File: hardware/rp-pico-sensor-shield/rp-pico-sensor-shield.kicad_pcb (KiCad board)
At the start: 2 copper layers, 87 x 65 mm, 36 parts, among them J1 Barrel_Jack, J10 Conn_01x04, J11 Conn_01x04, J12 Conn_01x04, J13 Conn_01x04, J14 Conn_01x04, J15 Conn_01x04, J16 Conn_01x04, J17 Conn_01x04, J18 Conn_01x03, J19 Conn_01x03, J2 AGND, J20 Conn_01x03, J21 Conn_01x03, J22 Conn_01x03, J23 Conn_01x03, J24 SM04B-SRSS-TB, J25 Conn_01x04, J26 Conn_01x04, J27 Conn_01x03, J3 Conn_01x04, J4 Conn_01x04, J5 Conn_01x04, J6 Conn_01x04, J7 Conn_01x04, J8 Conn_01x04, J9 Conn_01x04, Q1 DMG2305UX, SW1 SW_Push, U1 Pico, U2 NCP1117-5.0_SOT223

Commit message: tweaks
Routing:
- net GND: track 448.1 -> 461.9 mm, vias 0 -> 1
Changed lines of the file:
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@@
   )
   (segment (start 117.6113 77.1685) (end 113.7798 81) (width 0.8) (layer "F.Cu") (net 1))
-  (segment (start 117.6113 76.631) (end 117.6113 77.1685) (width 0.8) (layer "F.Cu") (net 1))
+  (segment (start 117.6113 77.1685) (end 117.6113 76.631) (width 0.8) (layer "F.Cu") (net 1))
+  (segment (start 117.6113 76.631) (end 123.3586 70.8837) (width 0.8) (layer "F.Cu") (net 1))
   (segment (start 113.7798 81) (end 113.3048 81) (width 0.8) (layer "F.Cu") (net 1))
-  (segment (start 117.6113 76.631) (end 123.3586 70.8837) (width 0.8) (layer "F.Cu") (net 1))
   (segment (start 113.4214 76.631) (end 117.6113 76.631) (width 0.8) (layer "F.Cu") (net 1))
   (segment (start 107.696 80.6516) (end 108.8852 79.4624) (width 0.5) (layer "F.Cu") (net 2))
-  (segment (start 122.936 82.55) (end 122.301 83.185) (width 0.5) (layer "F.Cu") (net 2))
   (segment (start 109.728 82.55) (end 108.204 82.55) (width 0.5) (layer "F.Cu") (net 2))
-  (segment (start 122.301 83.185) (end 122.301 87.757) (width 0.5) (layer "F.Cu") (net 2))
   (segment (start 132.969 97.902) (end 132.371 98.5) (width 0.5) (layer "F.Cu") (net 2))
-  (segment (start 132.969 92.583) (end 132.969 97.902) (width 0.5) (layer "F.Cu") (net 2))
+  (segment (start 132.969 92.583) (end 132.969 97.79) (width 0.5) (layer "F.Cu") (net 2))
   (segment (start 132.371 98.5) (end 131.0963 98.5) (width 0.5) (layer "F.Cu") (net 2))
-  (segment (start 113.3048 79.45) (end 112.828 79.45) (width 0.5) (layer "F.Cu") (net 2))
+  (segment (start 108.8852 78.3128) (end 108.8852 76.6948) (width 0.5) (layer "F.Cu") (net 2))
   (segment (start 131.318 90.932) (end 132.969 92.583) (width 0.5) (layer "F.Cu") (net 2))
   (segment (start 68.8808 73.66) (end 69.6184 74.3976) (width 0.8) (layer "F.Cu") (net 2))
   (segment (start 57.656 73.66) (end 68.8808 73.66) (width 0.8) (layer "F.Cu") (net 2))
-  (segment (start 122.936 82.55) (end 123.486 82) (width 0.5) (layer "F.Cu") (net 2))
+  (segment (start 125.6548 82) (end 122.301 85.3538) (width 0.8) (layer "F.Cu") (net 2))
   (segment (start 69.6184 74.3976) (end 69.6184 76.0476) (width 0.8) (layer "F.Cu") (net 2))
   (segment (start 125.476 90.932) (end 131.318 90.932) (width 0.5) (layer "F.Cu") (net 2))
+  (segment (start 122.301 85.3538) (end 122.301 86.741) (width 0.8) (layer "F.Cu") (net 2))
+  (segment (start 129.3586 70.8837) (end 129.3586 78.2962) (width 0.8) (layer "F.Cu") (net 2))
+  (segment (start 129.3586 78.2962) (end 125.6548 82) (width 0.8) (layer "F.Cu") (net 2))
   (segment (start 108.204 82.55) (end 107.696 82.042) (width 0.5) (layer "F.Cu") (net 2))
   (segment (start 56.9184 74.3976) (end 57.656 73.66) (width 0.8) (layer "F.Cu") (net 2))
-  (segment (start 123.486 82) (end 125.6548 82) (width 0.5) (layer "F.Cu") (net 2))
+  (segment (start 109.877999 82.400001) (end 112.828 79.45) (width 0.8) (layer "F.Cu") (net 2))
   (segment (start 122.301 87.757) (end 125.476 90.932) (width 0.5) (layer "F.Cu") (net 2))
-  (segment (start 108.8852 79.4624) (end 108.8852 76.6948) (width 0.5) (layer "F.Cu") (net 2))
-  (segment (start 112.828 79.45) (end 109.728 82.55) (width 0.5) (layer "F.Cu") (net 2))
+  (segment (start 122.301 86.741) (end 122.301 87.757) (width 0.5) (layer "F.Cu") (net 2))
+  (segment (start 108.8852 79.4624) (end 108.8852 78.4052) (width 0.5) (layer "F.Cu") (net 2))
+  (segment (start 107.696 81.534) (end 107.696 80.6516) (width 0.5) (layer "F.Cu") (net 2))
+  (segment (start 125.254799 82.400001) (end 109.877999 82.400001) (width 0.8) (layer "F.Cu") (net 2))
   (segment (start 108.8852 76.6948) (end 108.8214 76.631) (width 0.5) (layer "F.Cu") (net 2))
-  (segment (start 107.696 82.042) (end 107.696 80.6516) (width 0.5) (layer "F.Cu") (net 2))
-  (segment (start 109.728 82.55) (end 122.936 82.55) (width 0.5) (layer "F.Cu") (net 2))
+  (segment (start 132.969 97.79) (end 132.969 97.902) (width 0.5) (layer "F.Cu") (net 2))
+  (segment (start 107.696 82.042) (end 107.696 81.534) (width 0.5) (layer "F.Cu") (net 2))
+  (segment (start 112.828 79.45) (end 113.3048 79.45) (width 0.8) (layer "F.Cu") (net 2))
   (segment (start 56.9184 76.0476) (end 56.9184 74.3976) (width 0.8) (layer "F.Cu") (net 2))
+  (segment (start 125.6548 82) (end 125.254799 82.400001) (width 0.8) (layer "F.Cu") (net 2))
+  (via (at 122.301 86.741) (size 0.8) (drill 0.4) (layers "F.Cu" "B.Cu") (net 2))
   (segment (start 124.206 113.411) (end 133.35 104.267) (width 0.8) (layer "B.Cu") (net 2))
   (segment (start 129.3586 70.8837) (end 129.3586 78.0838) (width 0.8) (layer "B.Cu") (net 2))
@@
   (segment (start 107.851919 83.400001) (end 112.229 83.4) (width 0.8) (layer "F.Cu") (net 9))
   (segment (start 106.426 65.184032) (end 106.426 81.974082) (width 0.8) (layer "F.Cu") (net 9))
+  (segment (start 110.2654 105.54) (end 107.7254 105.54) (width 0.8) (layer "F.Cu") (net 9))
   (segment (start 64.008 54.102) (end 65.19 52.92) (width 0.8) (layer "F.Cu") (net 9))
   (segment (start 89.905 90.54) (end 81.7254 90.54) (width 0.8) (layer "B.Cu") (net 9))
@@
   (segment (start 81.7254 105.54) (end 79.1854 105.54) (width 0.8) (layer "B.Cu") (net 9))
   (segment (start 76.6454 105.54) (end 71.2654 105.54) (width 0.8) (layer "B.Cu") (net 9))
-  (segment (start 110.2654 105.54) (end 107.7254 105.54) (width 0.8) (layer "B.Cu") (net 9))
   (segment (start 79.1854 90.54) (end 81.7254 90.54) (width 0.8) (layer "B.Cu") (net 9))
   (segment (start 111.125 96.012) (end 95.377 96.012) (width 0.8) (layer "B.Cu") (net 9))
@@
   (segment (start 94.049 84.143) (end 92.4784 82.5724) (width 0.25) (layer "F.Cu") (net 19))
   (segment (start 94.499 84.963) (end 97.5584 81.9036) (width 0.25) (layer "F.Cu") (net 20))
+  (segment (start 104.873 106.905) (end 103.886 105.918) (width 0.25) (layer "F.Cu") (net 20))
+  (segment (start 101.473 99.820604) (end 99.569396 99.820604) (width 0.25) (layer "F.Cu") (net 20))
+  (segment (start 106.5504 106.905) (end 104.873 106.905) (width 0.25) (layer "F.Cu") (net 20))
   (segment (start 97.5584 81.9036) (end 97.5584 76.0476) (width 0.25) (layer "F.Cu") (net 20))
   (segment (start 94.499 94.750208) (end 94.499 84.963) (width 0.25) (layer "F.Cu") (net 20))
   (segment (start 99.569396 99.820604) (end 94.499 94.750208) (width 0.25) (layer "F.Cu") (net 20))
-  (segment (start 107.7254 108.08) (end 106.3604 106.715) (width 0.25) (layer "F.Cu") (net 20))
-  (segment (start 106.3604 106.715) (end 106.3604 102.513299) (width 0.25) (layer "F.Cu") (net 20))
-  (segment (start 103.667705 99.820604) (end 99.569396 99.820604) (width 0.25) (layer "F.Cu") (net 20))
-  (segment (start 106.3604 102.513299) (end 103.667705 99.820604) (width 0.25) (layer "F.Cu") (net 20))
+  (segment (start 107.7254 108.08) (end 106.5504 106.905) (width 0.25) (layer "F.Cu") (net 20))
+  (segment (start 103.886 105.918) (end 103.886 101.979604) (width 0.25) (layer "F.Cu") (net 20))
+  (segment (start 103.886 101.979604) (end 101.727 99.820604) (width 0.25) (layer "F.Cu") (net 20))
+  (segment (start 101.727 99.820604) (end 101.473 99.820604) (width 0.25) (layer "F.Cu") (net 20))
   (segment (start 94.949 94.563812) (end 94.949 85.149396) (width 0.25) (layer "F.Cu") (net 21))
-  (segment (start 109.0904 102.703299) (end 105.757705 99.370604) (width 0.25) (layer "F.Cu") (net 21))
-  (segment (start 105.757705 99.370604) (end 99.755792 99.370604) (width 0.25) (layer "F.Cu") (net 21))
-  (segment (start 109.0904 106.905) (end 109.0904 102.703299) (width 0.25) (layer "F.Cu") (net 21))
+  (segment (start 107.186796 106.905) (end 106.426 106.144204) (width 0.25) (layer "F.Cu") (net 21))
+  (segment (start 109.0904 106.905) (end 107.186796 106.905) (width 0.25) (layer "F.Cu") (net 21))
+  (segment (start 103.217705 99.370604) (end 99.755792 99.370604) (width 0.25) (layer "F.Cu") (net 21))
+  (segment (start 106.426 102.578899) (end 103.217705 99.370604) (width 0.25) (layer "F.Cu") (net 21))
+  (segment (start 106.426 106.144204) (end 106.426 102.578899) (width 0.25) (layer "F.Cu") (net 21))
+  (segment (start 94.949 85.149396) (end 100.0984 79.999996) (width 0.25) (layer "F.Cu") (net 21))
   (segment (start 110.2654 108.08) (end 109.0904 106.905) (width 0.25) (layer "F.Cu") (net 21))
-  (segment (start 94.949 85.149396) (end 100.0984 79.999996) (width 0.25) (layer "F.Cu") (net 21))
   (segment (start 100.0984 79.999996) (end 100.0984 76.0476) (width 0.25) (layer "F.Cu") (net 21))
   (segment (start 99.755792 99.370604) (end 94.949 94.563812) (width 0.25) (layer "F.Cu") (net 21))

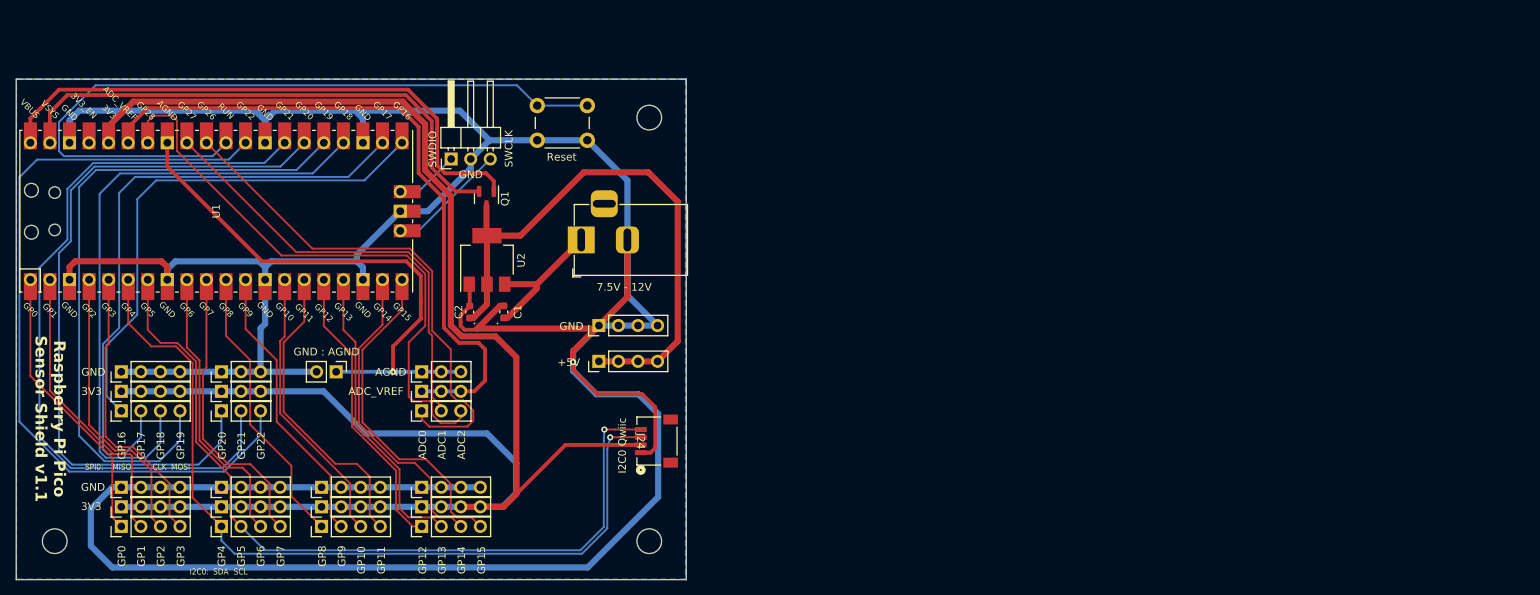
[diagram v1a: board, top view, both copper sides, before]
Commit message: finalized pin wiring
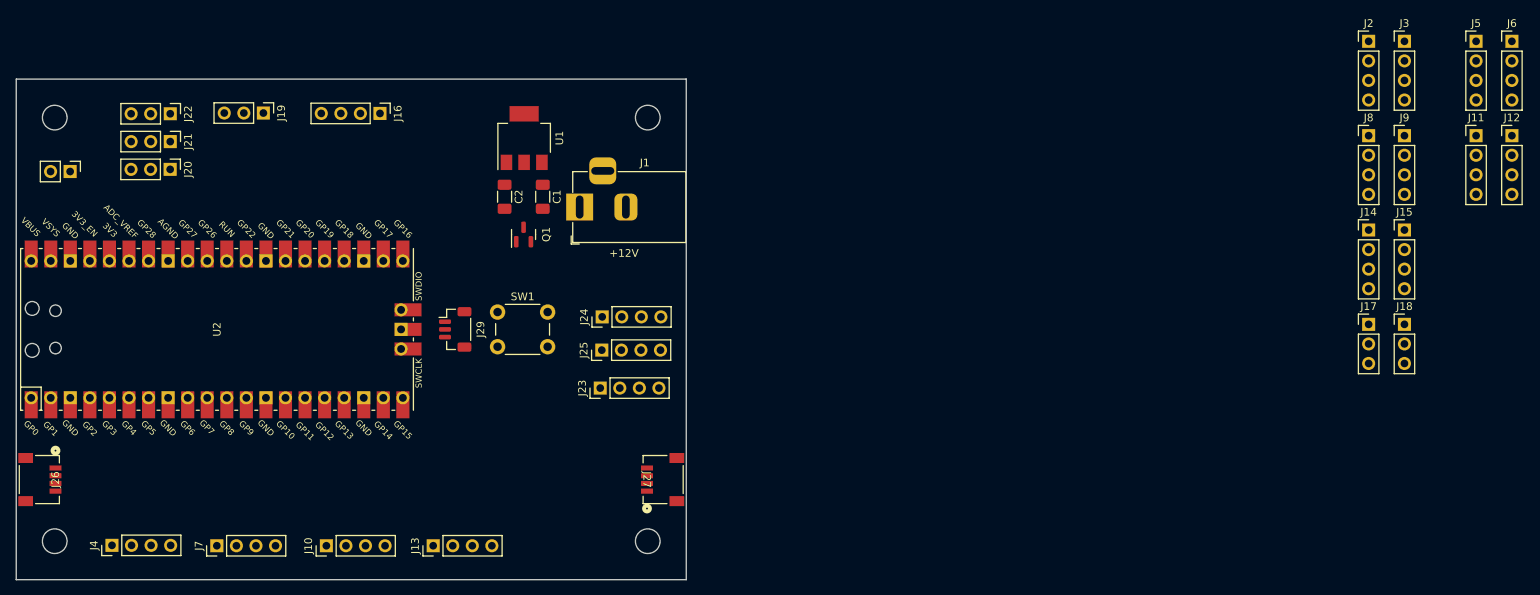
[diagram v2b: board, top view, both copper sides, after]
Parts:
- removed the REF** at (132.2, 110.0)
- removed the REF** at (132.2, 55.0)
- added J28: AGND, Connector_PinHeader_2.54mm:PinHeader_1x02_P2.54mm_Vertical, F.Cu at (57.0, 62.0)
- added J29: Conn_01x03, Connector_JST:JST_SH_BM03B-SRSS-TB_1x03-1MP_P1.00mm_Vertical, F.Cu at (107.0, 82.5)
- added REF**: MountingHole_3.2mm_M3, MountingHole:MountingHole_3.2mm_M3, F.Cu at (55.0, 55.0)
- added REF**: MountingHole_3.2mm_M3, MountingHole:MountingHole_3.2mm_M3, F.Cu at (132.0, 110.0)
- added REF**: MountingHole_3.2mm_M3, MountingHole:MountingHole_3.2mm_M3, F.Cu at (132.0, 55.0)
- C1, C2: footprint Capacitor_SMD:C_0603_1608Metric -> Capacitor_SMD:C_1206_3216Metric_Pad1.33x1.80mm_HandSolder
- J17: value Conn_01x04 -> Conn_01x03; footprint Connector_PinHeader_2.54mm:PinHeader_1x04_P2.54mm_Vertical -> Connector_PinHeader_2.54mm:PinHeader_1x03_P2.54mm_Vertical
- J2: value AGND -> Conn_01x04; footprint Connector_PinHeader_2.54mm:PinHeader_1x02_P2.54mm_Vertical -> Connector_PinHeader_2.54mm:PinHeader_1x04_P2.54mm_Vertical
- J23: value Conn_01x03 -> Conn_01x04; footprint Connector_PinHeader_2.54mm:PinHeader_1x03_P2.54mm_Vertical -> Connector_PinHeader_2.54mm:PinHeader_1x04_P2.54mm_Vertical
- J24: value SM04B-SRSS-TB -> Conn_01x04; footprint SM04B-SRSS-TB:CONN_SM04B-SRSS-TB_JST -> Connector_PinHeader_2.54mm:PinHeader_1x04_P2.54mm_Vertical
- J26: value Conn_01x04 -> I2C0; footprint Connector_PinHeader_2.54mm:PinHeader_1x04_P2.54mm_Vertical -> SM04B-SRSS-TB:CONN_SM04B-SRSS-TB_JST
- J27: value Conn_01x03 -> I2C1; footprint Connector_PinHeader_2.54mm:PinHeader_1x03_P2.54mm_Horizontal -> SM04B-SRSS-TB:CONN_SM04B-SRSS-TB_JST
- U1: value Pico -> NCP1117-5.0_SOT223; footprint MCU_RaspberryPi_and_Boards:RPi_Pico_SMD_TH -> Package_TO_SOT_SMD:SOT-223-3_TabPin2
- U2: value NCP1117-5.0_SOT223 -> Pico; footprint Package_TO_SOT_SMD:SOT-223-3_TabPin2 -> MCU_RaspberryPi_and_Boards:RPi_Pico_SMD_TH
- moved J5 185.2 mm to (239.6, 45.1), turned to 0 degrees
- moved J3 178.1 mm to (230.3, 45.1), turned to 0 degrees
- moved J6 177.3 mm to (244.2, 45.1), turned to 0 degrees
- moved J15 167.6 mm to (230.3, 69.6), turned to 0 degrees
- moved J17 162.3 mm to (225.6, 81.8), turned to 0 degrees
- moved J11 158.3 mm to (239.6, 57.3), turned to 0 degrees
- moved J8 157.4 mm to (225.6, 57.3), turned to 0 degrees
- moved J18 154.0 mm to (230.3, 81.8), turned to 0 degrees
- moved J12 148.7 mm to (244.2, 57.3), turned to 0 degrees
- moved J9 147.8 mm to (230.3, 57.3), turned to 0 degrees
- moved J2 140.8 mm to (225.6, 45.1), turned to 0 degrees
- moved J14 128.8 mm to (225.6, 69.6), turned to 0 degrees
- moved J26 75.4 mm to (53.0, 102.0)
- moved J27 49.9 mm to (134.0, 102.0), turned to -90 degrees
- moved J16 49.3 mm to (97.2, 54.5), turned to -90 degrees
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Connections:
- C1 pad 1: Net-(U2-VI) -> +12V
- J1 pad 1: Net-(U2-VI) -> +12V
- J10 pad 1: +3.3V -> GPIO8
- J10 pad 2: +3.3V -> GPIO9
- J10 pad 3: +3.3V -> GPIO10
- J10 pad 4: +3.3V -> GPIO11
- J11 pad 1: GPIO8 -> GND
- J11 pad 2: GPIO9 -> GND
- J11 pad 3: GPIO10 -> GND
- J11 pad 4: GPIO11 -> GND
- J12 pad 1: GND -> +3.3V
- J12 pad 2: GND -> +3.3V
- J12 pad 3: GND -> +3.3V
- J12 pad 4: GND -> +3.3V
- J13 pad 1: +3.3V -> GPIO12
- J13 pad 2: +3.3V -> GPIO13
- J13 pad 3: +3.3V -> GPIO14
- J13 pad 4: +3.3V -> GPIO15
- J14 pad 1: GPIO12 -> GND
- J14 pad 2: GPIO13 -> GND
- J14 pad 3: GPIO14 -> GND
- J14 pad 4: GPIO15 -> GND
- J15 pad 1: GND -> +3.3V
- J15 pad 2: GND -> +3.3V
- J15 pad 3: GND -> +3.3V
- J15 pad 4: GND -> +3.3V
- J16 pad 1: +3.3V -> GPIO16
- J16 pad 2: +3.3V -> GPIO17
- J16 pad 3: +3.3V -> GPIO18
- J16 pad 4: +3.3V -> GPIO19
- J17 pad 1: GPIO16 -> GND
- J17 pad 2: GPIO17 -> GND
- J17 pad 3: GPIO18 -> GND
- J18 pad 1: GPIO20 -> +3.3V
- J18 pad 2: GPIO21 -> +3.3V
- J18 pad 3: GPIO22 -> +3.3V
- J19 pad 1: +3.3V -> GPIO20
- J19 pad 2: +3.3V -> GPIO21
- J19 pad 3: +3.3V -> GPIO22
- J2 pad 1: AGND -> GND
- J20 pad 1: GND -> AGND
- J20 pad 2: GND -> AGND
- J20 pad 3: GND -> AGND
- J21 pad 1: AGND -> ADC_VREF
- J21 pad 2: AGND -> ADC_VREF
- J21 pad 3: AGND -> ADC_VREF
- J22 pad 1: ADC_VREF -> ADC0
- J22 pad 2: ADC_VREF -> ADC1
- J22 pad 3: ADC_VREF -> ADC2
- J23 pad 1: ADC0 -> GND
- J23 pad 2: ADC1 -> GND
- J23 pad 3: ADC2 -> GND
- J24 pad 1: GND -> +12V
- J24 pad 2: +3.3V -> +12V
- J24 pad 3: GPIO4 -> +12V
- J24 pad 4: GPIO5 -> +12V
- J26 pad 2: GND -> +3.3V
- J26 pad 3: GND -> GPIO4
- J26 pad 4: GND -> GPIO5
- J27 pad 1: SWIO -> GND
- J27 pad 2: GND -> +3.3V
- J27 pad 3: SWCLK -> GPIO6
- J3 pad 1: GPIO0 -> +3.3V
- J3 pad 2: GPIO1 -> +3.3V
- J3 pad 3: GPIO2 -> +3.3V
- J3 pad 4: GPIO3 -> +3.3V
- J4 pad 1: +3.3V -> GPIO0
- J4 pad 2: +3.3V -> GPIO1
- J4 pad 3: +3.3V -> GPIO2
- J4 pad 4: +3.3V -> GPIO3
- J6 pad 1: GND -> +3.3V
- J6 pad 2: GND -> +3.3V
- J6 pad 3: GND -> +3.3V
- J6 pad 4: GND -> +3.3V
- J7 pad 1: +3.3V -> GPIO4
- J7 pad 2: +3.3V -> GPIO5
- J7 pad 3: +3.3V -> GPIO6
- J7 pad 4: +3.3V -> GPIO7
- J8 pad 1: GPIO4 -> GND
- J8 pad 2: GPIO5 -> GND
- J8 pad 3: GPIO6 -> GND
- J8 pad 4: GPIO7 -> GND
- J9 pad 1: GND -> +3.3V
- J9 pad 2: GND -> +3.3V
- J9 pad 3: GND -> +3.3V
- J9 pad 4: GND -> +3.3V
- U1 pad 1: GPIO0 -> GND
- U1 pad 2: GPIO1 -> +5V
- U1 pad 3: GND -> +12V
- U2 pad 1: GND -> GPIO0
- U2 pad 2: +5V -> GPIO1
- U2 pad 3: Net-(U2-VI) -> GND
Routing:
- net GND: track 461.9 -> 0.00 mm, vias 1 -> 0
- net +3.3V: track 236.6 -> 0.00 mm
- net GPIO4: track 108.8 -> 0.00 mm, vias 1 -> 0
- net GPIO5: track 105.3 -> 0.00 mm, vias 1 -> 0
- net GPIO22: track 102.0 -> 0.00 mm
- net GPIO21: track 98.3 -> 0.00 mm
- net RESET: track 98.1 -> 0.00 mm
- net GPIO20: track 94.4 -> 0.00 mm
- net ADC_VREF: track 88.5 -> 0.00 mm
- net GPIO19: track 85.9 -> 0.00 mm
- net GPIO18: track 81.0 -> 0.00 mm
- net GPIO17: track 80.6 -> 0.00 mm
- net ADC2: track 77.0 -> 0.00 mm
- net +5V: track 75.0 -> 0.00 mm
- net Net-(Q1-G): track 74.7 -> 0.00 mm
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- removed copper zone on B.Cu, net GND
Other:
- board text added: "+12V"
- board text removed: "+"
- board text removed: "+5V"
- board text removed: "3V3"
- board text removed: "7.5V - 12V"
- board text removed: "ADC0"
- board text removed: "ADC1"
- board text removed: "ADC2"
- board text removed: "ADC_VREF"
- board text removed: "AGND"
- board text removed: "CLK"
- board text removed: "GND"
- board text removed: "GND : AGND"
- board text removed: "GP0"
- board text removed: "GP1"
- board text removed: "GP10"
- board text removed: "GP11"
- board text removed: "GP12"
- board text removed: "GP13"
- board text removed: "GP14"
- board text removed: "GP15"
- board text removed: "GP16"
- board text removed: "GP17"
- board text removed: "GP18"
- board text removed: "GP19"
- board text removed: "GP2"
- board text removed: "GP20"
- board text removed: "GP21"
- board text removed: "GP22"
- board text removed: "GP3"
- board text removed: "GP4"
- board text removed: "GP5"
- board text removed: "GP6"
- board text removed: "GP7"
- board text removed: "GP8"
- board text removed: "GP9"
- board text removed: "I2C0 Qwiic"
- board text removed: "I2C0:"
- board text removed: "MISO"
- board text removed: "MOSI"
- board text removed: "Raspberry Pi Pico Sensor Shield v1.1"
- board text removed: "Reset"
- board text removed: "SCL"
- board text removed: "SDA"
- board text removed: "SPI0:"
- board text removed: "SWCLK"
- board text removed: "SWDIO"

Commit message: wip update to rp2040 sensor shield
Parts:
- J24: value Conn_01x04 -> Screw Terminal; footprint Connector_PinHeader_2.54mm:PinHeader_1x04_P2.54mm_Vertical -> CONN2_1760510000_WED:CONN2_1760510000_WED
- moved J3 175.7 mm to (64.2, 102.5), turned to 90 degrees
- moved J6 172.8 mm to (81.2, 102.5), turned to 90 degrees
- moved J2 170.4 mm to (64.2, 100.0), turned to 90 degrees
- moved J5 167.6 mm to (81.2, 100.0), turned to 90 degrees
- moved J18 147.2 mm to (84.3, 62.5), turned to -90 degrees
- moved J17 142.3 mm to (84.3, 65.0), turned to -90 degrees
- moved J9 139.5 mm to (98.2, 102.5), turned to 90 degrees
- moved J12 136.6 mm to (115.2, 102.5), turned to 90 degrees
- moved J8 134.3 mm to (98.2, 100.0), turned to 90 degrees
- moved J11 131.4 mm to (115.2, 100.0), turned to 90 degrees
- moved J15 129.1 mm to (101.3, 62.5), turned to -90 degrees
- moved J14 124.4 mm to (101.3, 65.0), turned to -90 degrees
- moved J23 15.9 mm to (110.0, 92.0)
- moved J13 12.4 mm to (115.2, 105.1)
- moved J10 9.70 mm to (98.2, 105.1)
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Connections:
- J24 pad 2: +12V -> GND
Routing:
- net GND: track 0.00 -> 380.3 mm
- net +3.3V: track 0.00 -> 223.4 mm
- net Net-(Q1-S): track 0.00 -> 89.9 mm
- net Net-(Q1-G): track 0.00 -> 86.2 mm
- net GPIO6: track 0.00 -> 79.1 mm, vias 0 -> 1
- net GPIO7: track 0.00 -> 74.8 mm, vias 0 -> 1
- net GPIO5: track 0.00 -> 61.7 mm
- net GPIO4: track 0.00 -> 60.0 mm
- net +5V: track 0.00 -> 55.5 mm
- net RESET: track 0.00 -> 48.9 mm
- net GPIO12: track 0.00 -> 36.3 mm
- net GPIO13: track 0.00 -> 35.5 mm
- net GPIO15: track 0.00 -> 34.8 mm
- net GPIO14: track 0.00 -> 32.9 mm
- net GPIO9: track 0.00 -> 31.5 mm
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- added copper zone on B.Cu, net GND
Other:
- board text added: "GP0"
- board text added: "GP1"
- board text added: "GP2"
- board text added: "GP3"
- board text added: "GP4"
- board text added: "GP5"
- board text added: "GP6"
- board text added: "GP7"
- board text added: "I2C0"
- board text added: "I2C1"
- board text added: "RESET"
- board text added: "Raspberry Pi Pico"
- board text added: "SWD"

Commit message: finalized sensor shield design
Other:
- board text added: "+5V"
- board text added: "3V3"
- board text added: "ADC0"
- board text added: "ADC1"
- board text added: "ADC2"
- board text added: "ADC_VREF"
- board text added: "AGND"
- board text added: "GND"
- board text added: "GP10"
- board text added: "GP11"
- board text added: "GP12"
- board text added: "GP13"
- board text added: "GP14"
- board text added: "GP15"
- board text added: "GP16"
- board text added: "GP17"
- board text added: "GP18"
- board text added: "GP19"
- board text added: "GP20"
- board text added: "GP21"
- board text added: "GP22"
- board text added: "GP4 GP5 GP6 GP7 GP19 GP16 GP18 GP17 GP0 GP1"
- board text added: "GP8"
- board text added: "GP9"
- board text added: "I2C0 SDA I2C0 SCL I2C1 SDA I2C1 SCL SPI0 TX SPI0 RX SPI0 SCK SPI0 CSn UART0 TX UART0 RX"
- board text added: "Interface"
- board text added: "Pins"
- board text added: "Raspberry Pi Pico Breakout Board"
- board text added: "SPI0"
- board text added: "UART0"
- board text added: "v1.2"
- board text added: "www.kamprath.net/hacks/"
- board text added: "©2024 by Michael Kamprath"
